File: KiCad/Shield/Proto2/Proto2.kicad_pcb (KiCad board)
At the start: 2 copper layers, 204.1 x 93.3 mm, 69 parts, among them J1 CONN_02X20, J10 CONN_01X02, J11 CONN_01X02, J14 GS2, J15 GS2, J17 GS2, J18 GS2, J19 GS2, J2 CONN_01X04, J20 GS2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

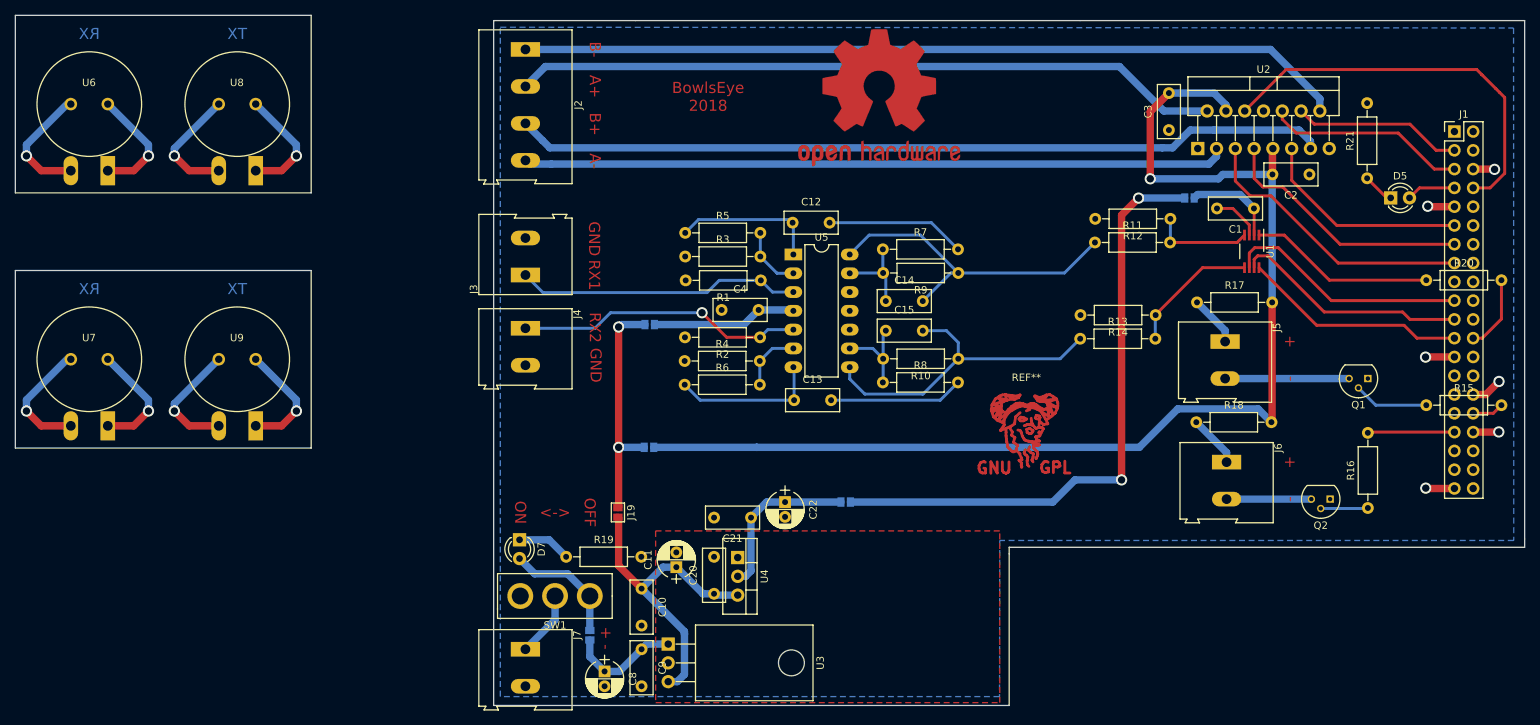
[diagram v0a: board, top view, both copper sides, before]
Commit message: Added proto2 kicad files
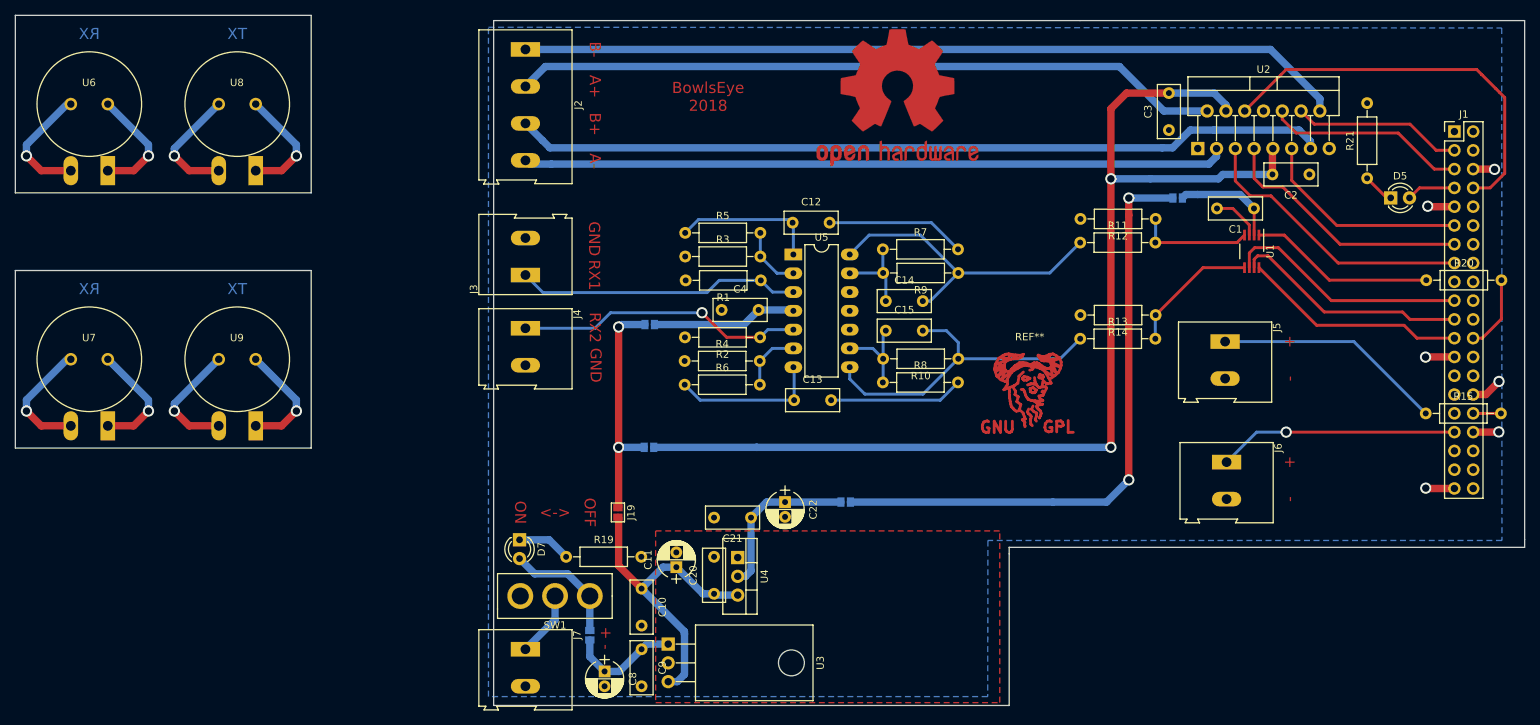
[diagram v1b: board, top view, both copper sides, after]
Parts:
- removed Q1, Q2: BFY51, TO_SOT_Packages_THT:TO-92_Molded_Narrow
- removed R16, R17, R18: R, Resistors_THT:R_Axial_DIN0207_L6.3mm_D2.5mm_P10.16mm_Horizontal
- R15: value R -> 0R
- moved REF** 5.52 mm to (154.2, 89.5)
- moved REF*** 2.47 mm to (136.3, 51.1)
- moved R11 2.00 mm to (161.0, 70.7)
- moved R12 2.00 mm to (171.2, 67.5)
- moved J18 1.60 mm to (174.2, 64.7)
- moved R15 1.12 mm to (207.7, 93.8)
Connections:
- J5 pad 2: Net-(J5-Pad2) -> GNDD
- J6 pad 1: Net-(J6-Pad1) -> ULTRA_TX2
- J6 pad 2: Net-(J6-Pad2) -> GNDD
- R15 pad 1: Net-(Q1-Pad2) -> Net-(J5-Pad1)
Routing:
- net Net-(J5-Pad1): track 6.87 -> 31.2 mm
- net ULTRA_TX2: track 11.7 -> 32.5 mm, vias 0 -> 1
- net Net-(J5-Pad2): track 16.8 -> 0.00 mm
- net Net-(J6-Pad2): track 11.5 -> 0.00 mm
- net +5V: track 257.1 -> 246.2 mm, vias 3 -> 4
- net Net-(Q1-Pad2): track 10.1 -> 0.00 mm
- net Net-(J6-Pad1): track 7.10 -> 0.00 mm
- net Net-(Q2-Pad2): track 6.40 -> 0.00 mm
- net ULTRA_RX1: track 13.7 -> 15.7 mm
- net Net-(C14-Pad2): track 44.5 -> 42.5 mm
- net +3V3: track 118.2 -> 119.8 mm
- net ULTRA_TX1: track 4.28 -> 3.76 mm

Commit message: Finished proto2 board
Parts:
- removed C14, C15: 10pF, Capacitors_THT:C_Rect_L7.2mm_W3.0mm_P5.00mm_FKS2_FKP2_MKS2_MKP2
- removed R11, R12, R13, R14: R, Resistors_THT:R_Axial_DIN0207_L6.3mm_D2.5mm_P10.16mm_Horizontal
- added D1: BAT48, Diodes_THT:D_T-1_P10.16mm_Horizontal, F.Cu at (158.5, 74.8)
- added D2: BAT48, Diodes_THT:D_T-1_P10.16mm_Horizontal, F.Cu at (148.3, 71.5)
- added D3: BAT48, Diodes_THT:D_T-1_P10.16mm_Horizontal, F.Cu at (158.5, 86.5)
- added D4: BAT48, Diodes_THT:D_T-1_P10.16mm_Horizontal, F.Cu at (148.3, 89.8)
- J7: value CONN_01X02 -> CONN_01X04; footprint Connectors_Terminal_Blocks:TerminalBlock_Altech_AK300-2_P5.00mm -> Connectors_Molex:Molex_KK-41791-04_04x3.96mm_Straight
- R10, R5, R6, R9: value 100K -> 500K
- moved REF** 13.4 mm to (144.4, 98.7)
- moved J7 7.99 mm to (87.4, 117.8)
- moved R19 6.74 mm to (93.7, 106.8)
- moved SW1 6.46 mm to (90.0, 112.0)
- moved D7 5.81 mm to (85.2, 105.1)
- moved REF*** 1.44 mm to (137.7, 51.0)
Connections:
- J7 pad 2: GNDD -> Net-(J7-Pad2)
- R10 pad 1: Net-(C15-Pad2) -> ULTRA_RX2
- R9 pad 1: Net-(C14-Pad2) -> ULTRA_RX1
- U5 pad 14: Net-(C14-Pad2) -> ULTRA_RX1
- U5 pad 8: Net-(C15-Pad2) -> ULTRA_RX2
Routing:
- net ULTRA_RX2: track 17.9 -> 69.8 mm, vias 0 -> 1
- net ULTRA_RX1: track 15.7 -> 60.8 mm, vias 0 -> 1
- net Net-(C15-Pad2): track 44.4 -> 0.00 mm
- net Net-(C14-Pad2): track 42.5 -> 0.00 mm
- net +Vs: track 31.5 -> 37.6 mm
- net Net-(R10-Pad2): track 12.3 -> 8.32 mm
- net Net-(R7-Pad1): track 11.7 -> 8.26 mm
- net +3V3: track 119.8 -> 117.8 mm
- net Net-(J7-Pad1): track 8.86 -> 6.88 mm
- net Net-(D7-Pad1): track 7.25 -> 9.17 mm

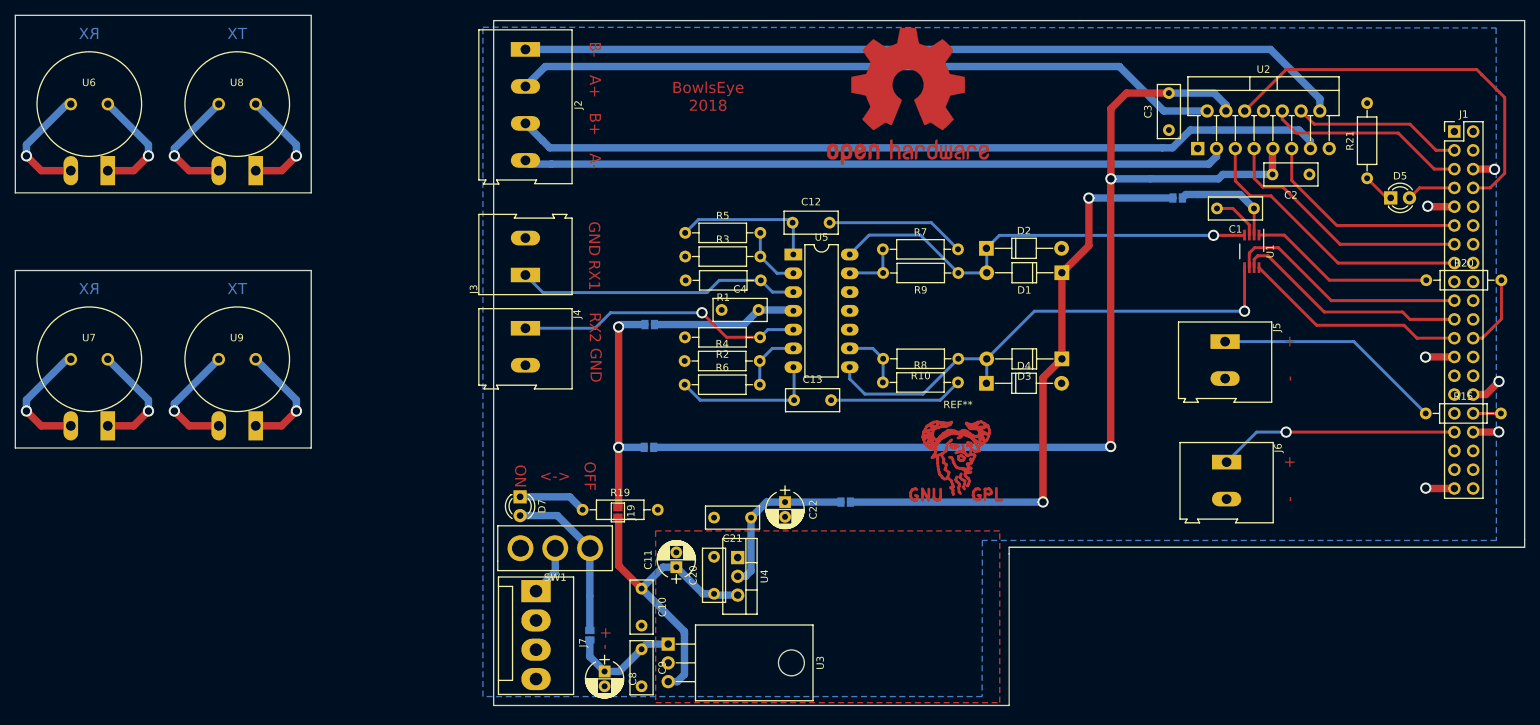
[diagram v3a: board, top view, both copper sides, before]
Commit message: added pngs of pcbs
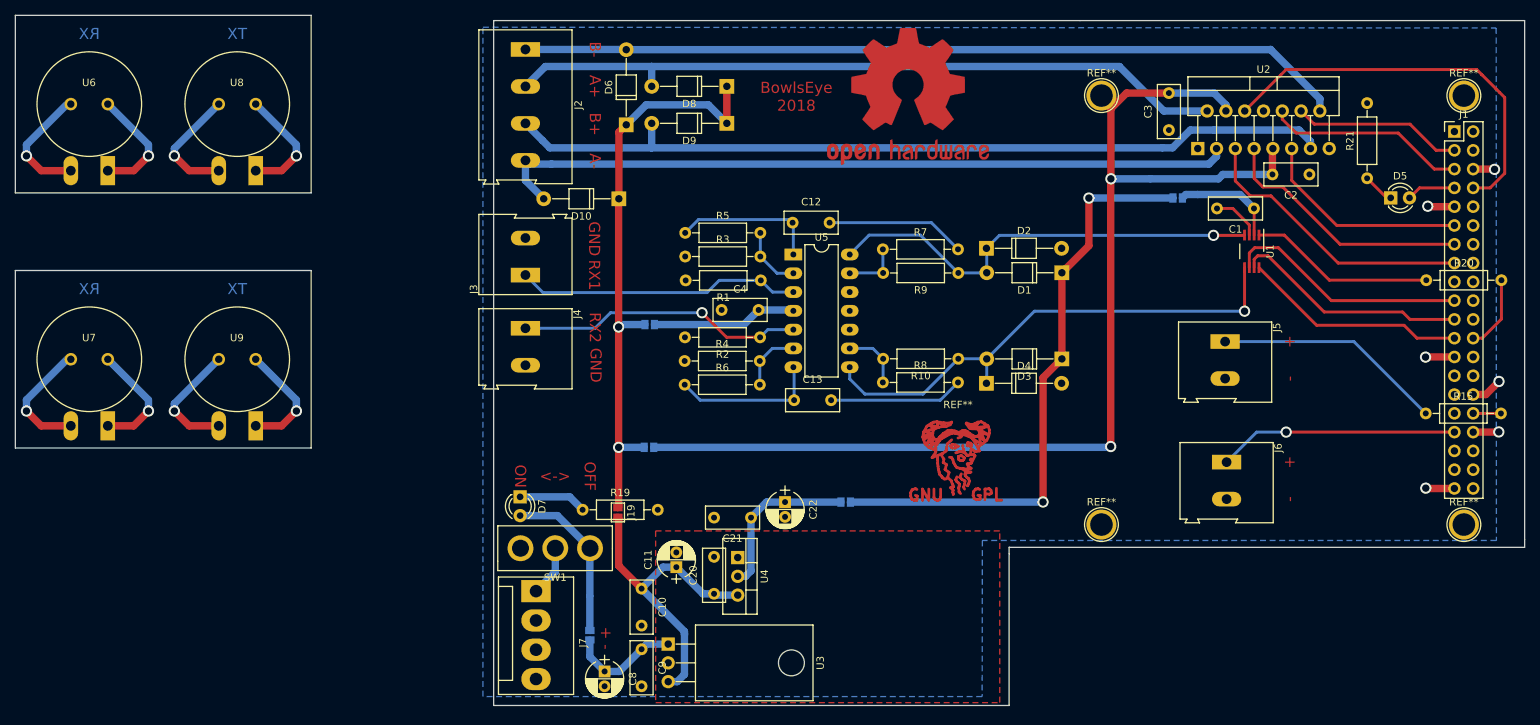
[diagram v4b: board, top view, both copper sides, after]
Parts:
- added D10: 1N4007, Diodes_THT:D_T-1_P10.16mm_Horizontal, F.Cu at (98.6, 64.8)
- added D6: 1N4007, Diodes_THT:D_T-1_P10.16mm_Horizontal, F.Cu at (99.6, 54.8)
- added D8: 1N4007, Diodes_THT:D_T-1_P10.16mm_Horizontal, F.Cu at (113.2, 49.6)
- added D9: 1N4007, Diodes_THT:D_T-1_P10.16mm_Horizontal, F.Cu at (113.2, 54.6)
- added REF**: 1pin, Connectors:1pin, F.Cu at (163.8, 108.8)
- added REF**: 1pin, Connectors:1pin, F.Cu at (212.8, 108.8)
- added REF**: 1pin, Connectors:1pin, F.Cu at (163.8, 50.9)
- added REF**: 1pin, Connectors:1pin, F.Cu at (212.8, 50.9)
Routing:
- net +5V: track 246.0 -> 294.6 mm
- net PHASE_A-: track 95.1 -> 101.4 mm
- net PHASE_B: track 110.1 -> 113.6 mm
- net PHASE_A: track 95.8 -> 98.6 mm
